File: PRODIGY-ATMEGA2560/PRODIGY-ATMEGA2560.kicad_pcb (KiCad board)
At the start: 4 copper layers, 55 x 40 mm, 29 parts, among them J1 DF40C-100DP-04V-51, J2 DF40C-100DP-04V-51, Q1 BC850, Q2 BC850, U1 ATmega2560-8A, U2 TXS0108EPW, U3 FT231XQ, Y1 8MHz

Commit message: major routing done on atmega board.
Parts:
- moved C8 0.18 mm to (114.9, 109.8)
- moved C7 0.15 mm to (121.9, 103.0)
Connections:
- U1 pad 15: /atmega2560/MOTOR_PWM_OUT_1 -> /atmega2560/DIGITAL_RGB_B
- U1 pad 16: /atmega2560/MOTOR_PWM_OUT_2 -> /atmega2560/DIGITAL_RGB_G
- U1 pad 19: /atmega2560/SPI_CS_BREAKOUT -> /atmega2560/SD_CS
- U1 pad 24: /atmega2560/DIGITAL_RGB_B -> /atmega2560/DIGITAL_RGB_R
- U1 pad 25: /atmega2560/DIGITAL_RGB_G -> /atmega2560/MOTOR_PWM_OUT_2
- U1 pad 26: /atmega2560/DIGITAL_RGB_R -> /atmega2560/MOTOR_PWM_OUT_1
- U1 pad 35: /atmega2560/MCU_GPIO_2 -> /atmega2560/MCU_GPIO_9
- U1 pad 36: /atmega2560/MCU_GPIO_3 -> /atmega2560/MCU_GPIO_11
- U1 pad 37: /atmega2560/MCU_GPIO_4 -> /atmega2560/MCU_GPIO_5
- U1 pad 38: /atmega2560/MCU_GPIO_5 -> /atmega2560/MCU_GPIO_6
- U1 pad 39: /atmega2560/MCU_GPIO_6 -> /atmega2560/MCU_GPIO_13
- U1 pad 40: /atmega2560/MCU_GPIO_7 -> /atmega2560/MCU_GPIO_26
- U1 pad 41: /atmega2560/MCU_GPIO_8 -> /atmega2560/MCU_GPIO_24
- U1 pad 42: /atmega2560/MCU_GPIO_9 -> /atmega2560/MCU_GPIO_8
- U1 pad 59: /atmega2560/SD_CS -> /atmega2560/SPI_CS_BREAKOUT
- U1 pad 60: /atmega2560/SD_EN -> /atmega2560/SD_DET_5V
- U1 pad 65: /atmega2560/SD_DET -> /atmega2560/SD_EN
- U1 pad 71: /atmega2560/MCU_GPIO_10 -> /atmega2560/MCU_GPIO_21
- U1 pad 72: /atmega2560/MCU_GPIO_11 -> /atmega2560/MCU_GPIO_16
- U1 pad 73: /atmega2560/MCU_GPIO_12 -> /atmega2560/MCU_GPIO_20
- U1 pad 74: /atmega2560/MCU_GPIO_13 -> /atmega2560/MCU_GPIO_12
- U1 pad 75: /atmega2560/MCU_GPIO_14 -> /atmega2560/MCU_GPIO_7
- U1 pad 77: /atmega2560/MCU_GPIO_16 -> /atmega2560/MCU_GPIO_14
- U1 pad 78: /atmega2560/MCU_GPIO_17 -> /atmega2560/MCU_GPIO_23
- U1 pad 82: /atmega2560/MCU_GPIO_20 -> /atmega2560/MCU_GPIO_25
- U1 pad 83: /atmega2560/MCU_GPIO_21 -> /atmega2560/MCU_GPIO_10
- U1 pad 85: /atmega2560/MCU_GPIO_23 -> /atmega2560/MCU_GPIO_27
- U1 pad 86: /atmega2560/MCU_GPIO_24 -> /atmega2560/MCU_GPIO_17
- U1 pad 87: /atmega2560/MCU_GPIO_25 -> /atmega2560/MCU_GPIO_4
- U1 pad 88: /atmega2560/MCU_GPIO_26 -> /atmega2560/MCU_GPIO_3
- U1 pad 89: /atmega2560/MCU_GPIO_27 -> /atmega2560/MCU_GPIO_2
- U1 pad 90: /atmega2560/ANALOG_PHOTOTRANSISTOR -> /atmega2560/ANALOG_BREAKOUT_PIEZO
- U1 pad 91: /atmega2560/ANALOG_JOYSTICK_X -> /atmega2560/ANALOG_BREAKOUT_PT100
- U1 pad 92: /atmega2560/ANALOG_JOYSTICK_Y -> /atmega2560/ANALOG_HEATER_TEMPERATURE
- U1 pad 93: /atmega2560/ANALOG_MICROPHONE -> /atmega2560/ANALOG_POTENTIOMETER
- U1 pad 94: /atmega2560/ANALOG_POTENTIOMETER -> /atmega2560/ANALOG_MICROPHONE
- U1 pad 95: /atmega2560/ANALOG_HEATER_TEMPERATURE -> /atmega2560/ANALOG_JOYSTICK_Y
- U1 pad 96: /atmega2560/ANALOG_BREAKOUT_PT100 -> /atmega2560/ANALOG_JOYSTICK_X
- U1 pad 97: /atmega2560/ANALOG_BREAKOUT_PIEZO -> /atmega2560/ANALOG_PHOTOTRANSISTOR
- U2 pad 1: /atmega2560/SD_DET -> /atmega2560/SD_CLK
- U2 pad 12: /atmega2560/SD_CS -> /atmega2560/SD_EN
- U2 pad 13: unconnected-(U2-B7-Pad13) -> /atmega2560/SD_DET_5V
- U2 pad 16: /atmega2560/SCK -> unconnected-(U2-B4-Pad16)
- U2 pad 18: /atmega2560/SD_EN -> /atmega2560/SD_CS
- U2 pad 20: /atmega2560/SD_DET -> /atmega2560/SCK
- U2 pad 3: /atmega2560/SD_Enable -> /atmega2560/SD_DAT3
- U2 pad 5: /atmega2560/SD_CLK -> /atmega2560/SD_DAT1
- U2 pad 7: /atmega2560/SD_DAT1 -> /atmega2560/SD_DAT2
- U2 pad 8: /atmega2560/SD_DAT2 -> /atmega2560/SD_DET
- U2 pad 9: /atmega2560/SD_DAT3 -> /atmega2560/SD_Enable
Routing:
- net /atmega2560/SD_DET_5V: track 0.00 -> 38.0 mm, vias 0 -> 2
- net /atmega2560/SD_EN: track 0.00 -> 36.8 mm, vias 0 -> 2
- net /atmega2560/SD_DAT1: track 0.00 -> 32.3 mm, vias 0 -> 1
- net /atmega2560/SD_DAT3: track 0.00 -> 31.2 mm, vias 0 -> 1
- net /atmega2560/MCU_GPIO_24: track 0.00 -> 31.1 mm, vias 0 -> 3
- net /atmega2560/SD_CLK: track 0.00 -> 30.7 mm, vias 0 -> 1
- net /atmega2560/SD_DAT2: track 0.00 -> 30.6 mm, vias 0 -> 1
- net /atmega2560/SD_DAT0: track 0.00 -> 30.5 mm, vias 0 -> 1
- net /atmega2560/SD_Enable: track 0.00 -> 30.2 mm, vias 0 -> 1
- net /atmega2560/MCU_RESET: track 18.3 -> 47.7 mm, vias 0 -> 1
- net /atmega2560/MCU_GPIO_8: track 0.00 -> 28.1 mm, vias 0 -> 3
- net /atmega2560/SD_CMD: track 0.00 -> 27.8 mm, vias 0 -> 1
- net /atmega2560/SD_DET: track 0.00 -> 27.4 mm, vias 0 -> 1
- net /atmega2560/SPI_CS_BREAKOUT: track 0.87 -> 27.6 mm, vias 1 -> 2
- net /atmega2560/MCU_GPIO_9: track 0.00 -> 25.9 mm, vias 0 -> 1
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
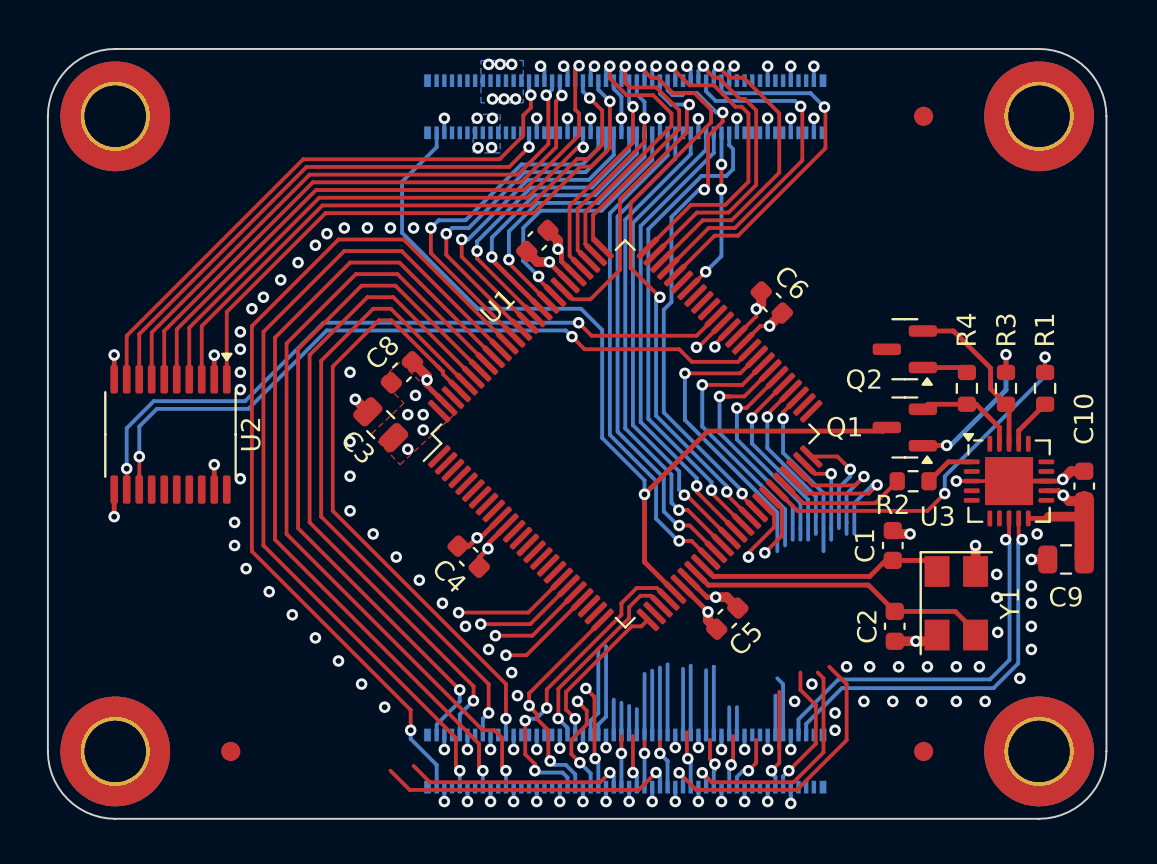
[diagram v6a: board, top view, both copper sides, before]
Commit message: Atmega board routing and power planes done. via stitching and labeling is needed
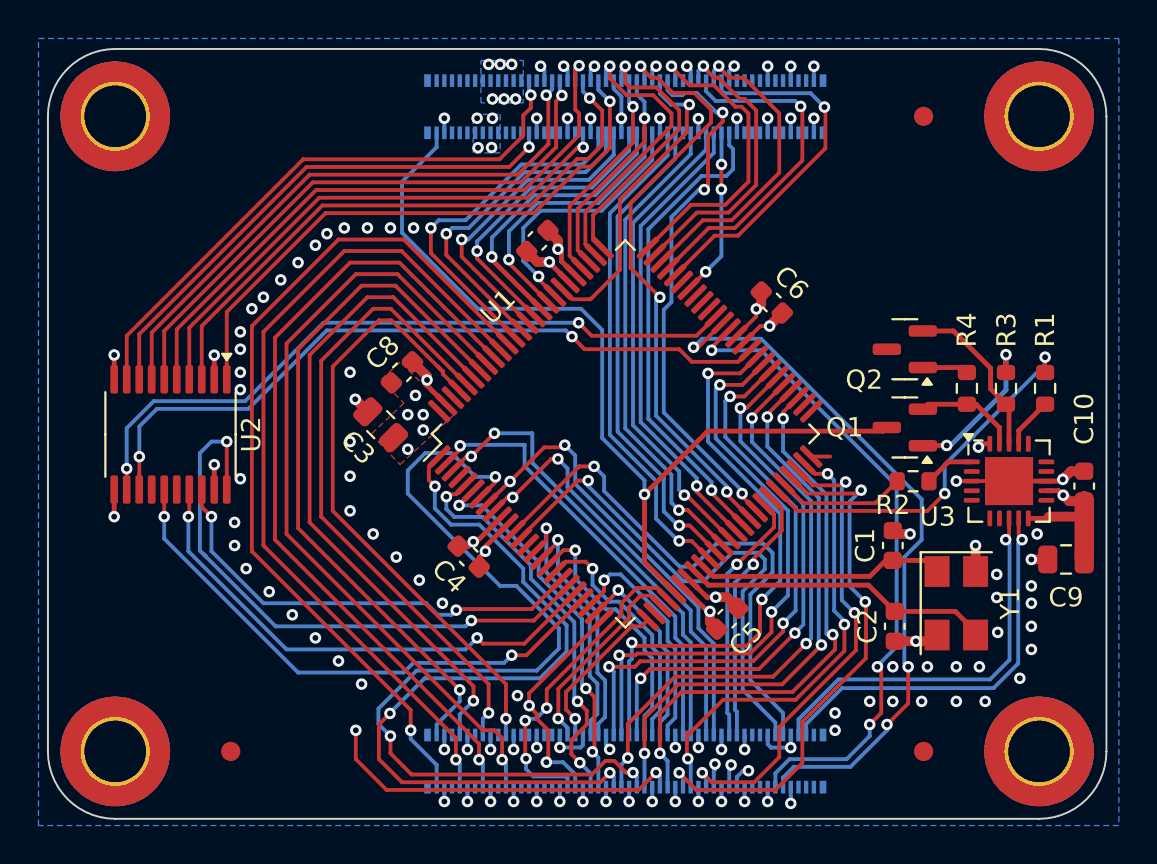
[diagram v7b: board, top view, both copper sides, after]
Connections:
- U1 pad 1: /atmega2560/DIGITAL_LED_OUT_2 -> /atmega2560/DIGITAL_HEATER_OUT
- U1 pad 15: /atmega2560/DIGITAL_RGB_B -> /atmega2560/DIGITAL_LED_OUT_1
- U1 pad 16: /atmega2560/DIGITAL_RGB_G -> /atmega2560/DIGITAL_LED_OUT_0
- U1 pad 17: /atmega2560/DIGITAL_LED_OUT_0 -> /atmega2560/DIGITAL_RGB_B
- U1 pad 18: /atmega2560/DIGITAL_LED_OUT_1 -> /atmega2560/DIGITAL_RGB_G
- U1 pad 47: /atmega2560/DIGITAL_BUTTON_IN_0 -> /atmega2560/SPI_CS_TFT
- U1 pad 48: /atmega2560/DIGITAL_BUTTON_IN_1 -> /atmega2560/SPI_CS_BREAKOUT
- U1 pad 49: /atmega2560/DIGITAL_BUTTON_IN_2 -> /atmega2560/SPI_CS_SEVENSEG
- U1 pad 50: /atmega2560/DIGITAL_BUTTON_IN_3 -> unconnected-(U1-PD7-Pad50)
- U1 pad 53: /atmega2560/SPI_CS_SEVENSEG -> /atmega2560/SPI_TFT_DC
- U1 pad 54: /atmega2560/SPI_CS_TFT -> /atmega2560/SPI_CS_NFC
- U1 pad 55: /atmega2560/SPI_TFT_DC -> /atmega2560/SPI_RST_NFC
- U1 pad 56: /atmega2560/SPI_TFT_RESET -> /atmega2560/DIGITAL_BUTTON_IN_0
- U1 pad 57: /atmega2560/SPI_CS_NFC -> /atmega2560/DIGITAL_BUTTON_IN_3
- U1 pad 58: /atmega2560/SPI_RST_NFC -> /atmega2560/DIGITAL_BUTTON_IN_2
- U1 pad 59: /atmega2560/SPI_CS_BREAKOUT -> /atmega2560/DIGITAL_BUTTON_IN_1
- U1 pad 6: /atmega2560/DIGITAL_HEATER_OUT -> /atmega2560/DIGITAL_LED_OUT_2
- U1 pad 7: /atmega2560/I2C_INTERRUPT_ACCEL -> /atmega2560/SPI_IRQ_NFC
- U1 pad 8: /atmega2560/I2C_INTERRUPT_KEYPAD -> /atmega2560/I2C_INTERRUPT_ACCEL
- U1 pad 9: /atmega2560/SPI_IRQ_NFC -> /atmega2560/I2C_INTERRUPT_KEYPAD
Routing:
- net /atmega2560/MISO: track 8.04 -> 54.7 mm, vias 2 -> 3
- net /atmega2560/MOSI: track 8.11 -> 54.6 mm, vias 2 -> 3
- net /atmega2560/SPI_IRQ_NFC: track 2.74 -> 47.5 mm, vias 1 -> 3
- net /atmega2560/SCK: track 7.97 -> 49.7 mm, vias 2 -> 3
- net /atmega2560/DIGITAL_HEATER_OUT: track 11.6 -> 40.9 mm, vias 1 -> 3
- net /atmega2560/SERIAL_OUT_TX2: track 8.88 -> 37.4 mm, vias 2 -> 3
- net /atmega2560/SERIAL_OUT_RX2: track 6.62 -> 34.2 mm, vias 2 -> 3
- net /atmega2560/SERIAL_OUT_RX1: track 3.07 -> 28.8 mm, vias 0 -> 1
- net /atmega2560/SERIAL_OUT_TX1: track 2.05 -> 27.3 mm, vias 0 -> 1
- net +3V3: track 2.56 -> 27.7 mm
- net /atmega2560/DIGITAL_BUTTON_IN_2: track 6.72 -> 30.2 mm, vias 1 -> 3
- net /atmega2560/DIGITAL_BUTTON_IN_3: track 7.45 -> 30.3 mm, vias 1 -> 3
- net /atmega2560/DIGITAL_BUTTON_IN_1: track 8.83 -> 30.2 mm, vias 1 -> 3
- net /atmega2560/DIGITAL_IR_EMITTER: track 3.60 -> 24.0 mm, vias 0 -> 2
- net /atmega2560/I2C_INTERRUPT_ACCEL: track 3.55 -> 23.6 mm, vias 0 -> 2
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- added copper zone on In1.Cu, net +5V
- added copper zone on B.Cu, net GND

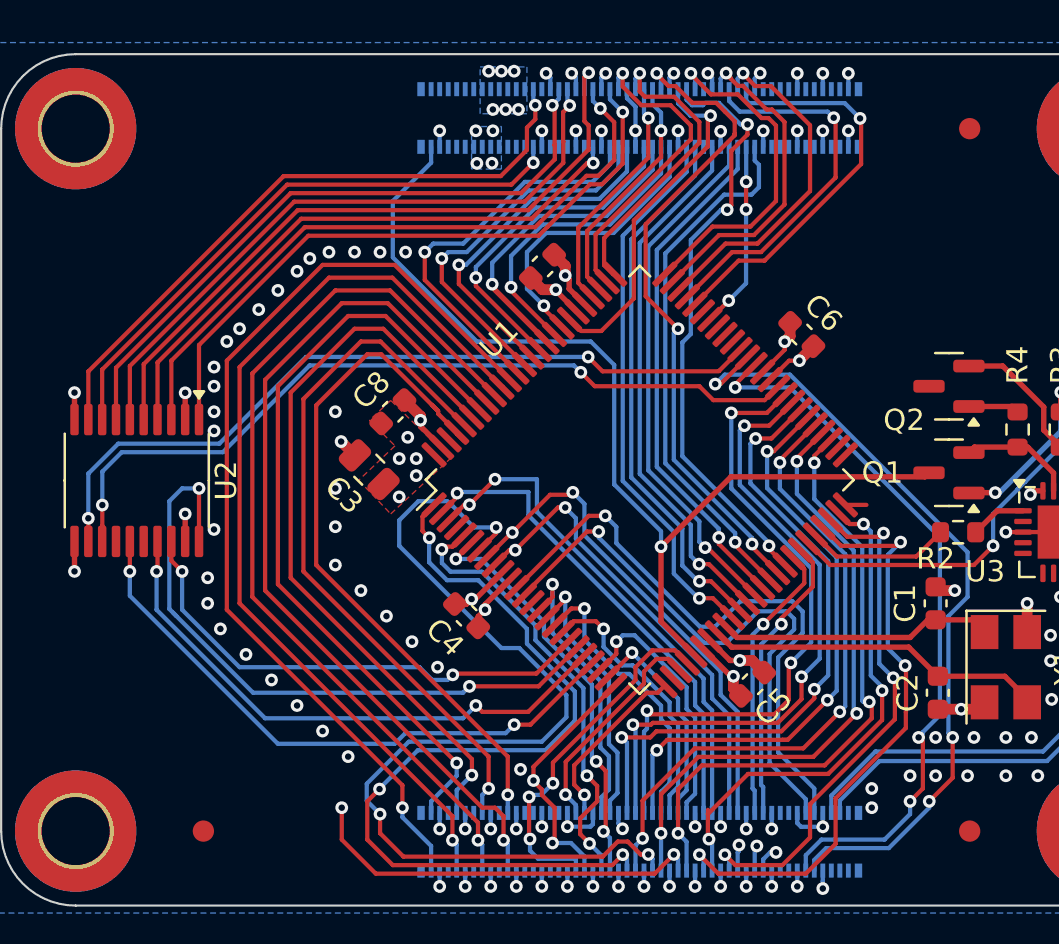
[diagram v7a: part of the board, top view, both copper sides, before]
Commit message: DRC ran with 0 errors
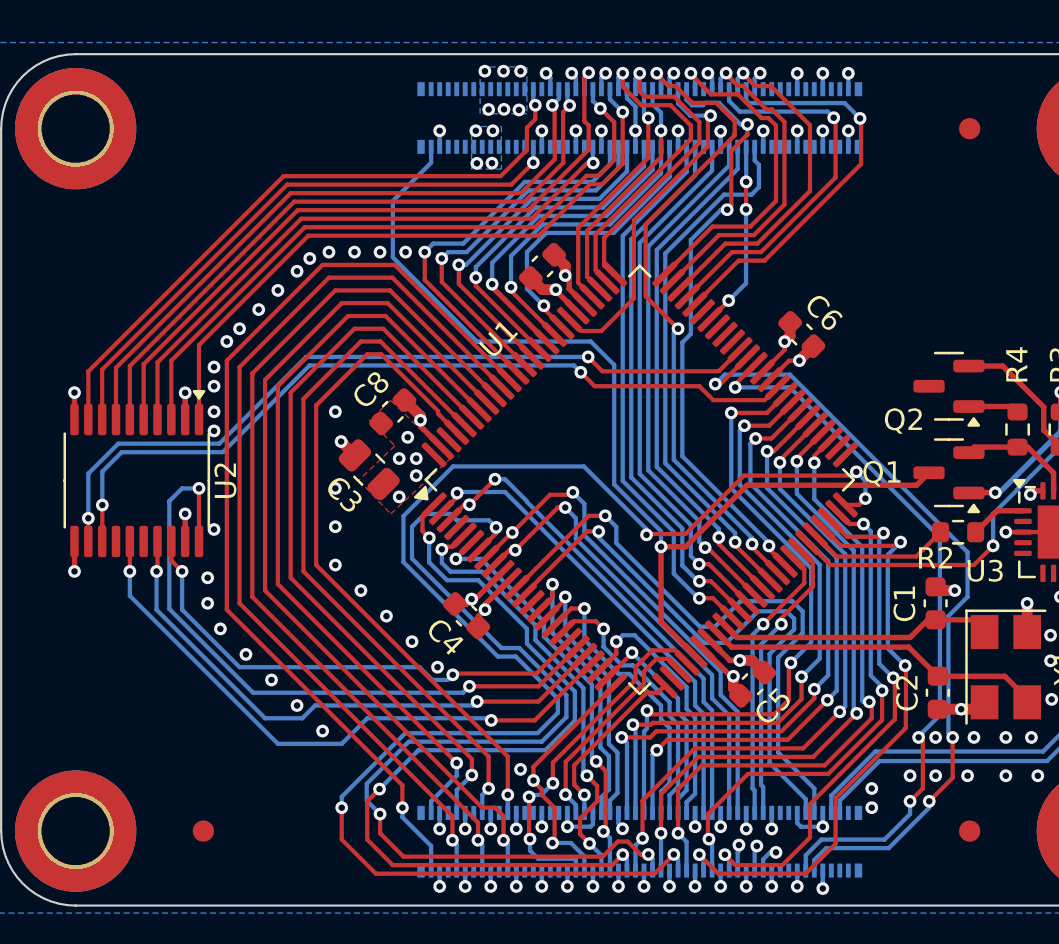
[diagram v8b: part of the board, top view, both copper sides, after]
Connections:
- U1 pad 50: unconnected-(U1-PD7-Pad50) -> /atmega2560/SPI_TFT_RESET
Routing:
- net /atmega2560/SPI_TFT_RESET: track 19.0 -> 71.6 mm, vias 2 -> 5
- net /atmega2560/SPI_IRQ_NFC: track 47.5 -> 46.0 mm
- net unconnected-(U1-PD7-Pad50): track 0.99 -> 0.00 mm
- net /atmega2560/MISO: track 54.7 -> 53.8 mm
- net /atmega2560/DIGITAL_IR_EMITTER: track 24.0 -> 23.1 mm
- net /atmega2560/DIGITAL_IR_RECEIVER: track 23.1 -> 22.4 mm
- net GND: vias 113 -> 112
